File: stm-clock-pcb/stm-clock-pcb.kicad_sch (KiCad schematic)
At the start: 22 parts, among them J2 LED connector, J3 SWD, J4 USB_C_Receptacle_PowerOnly_6P, U1 STM32F103C6Tx, U2 L78L33_SOT89, Y1 16MHz

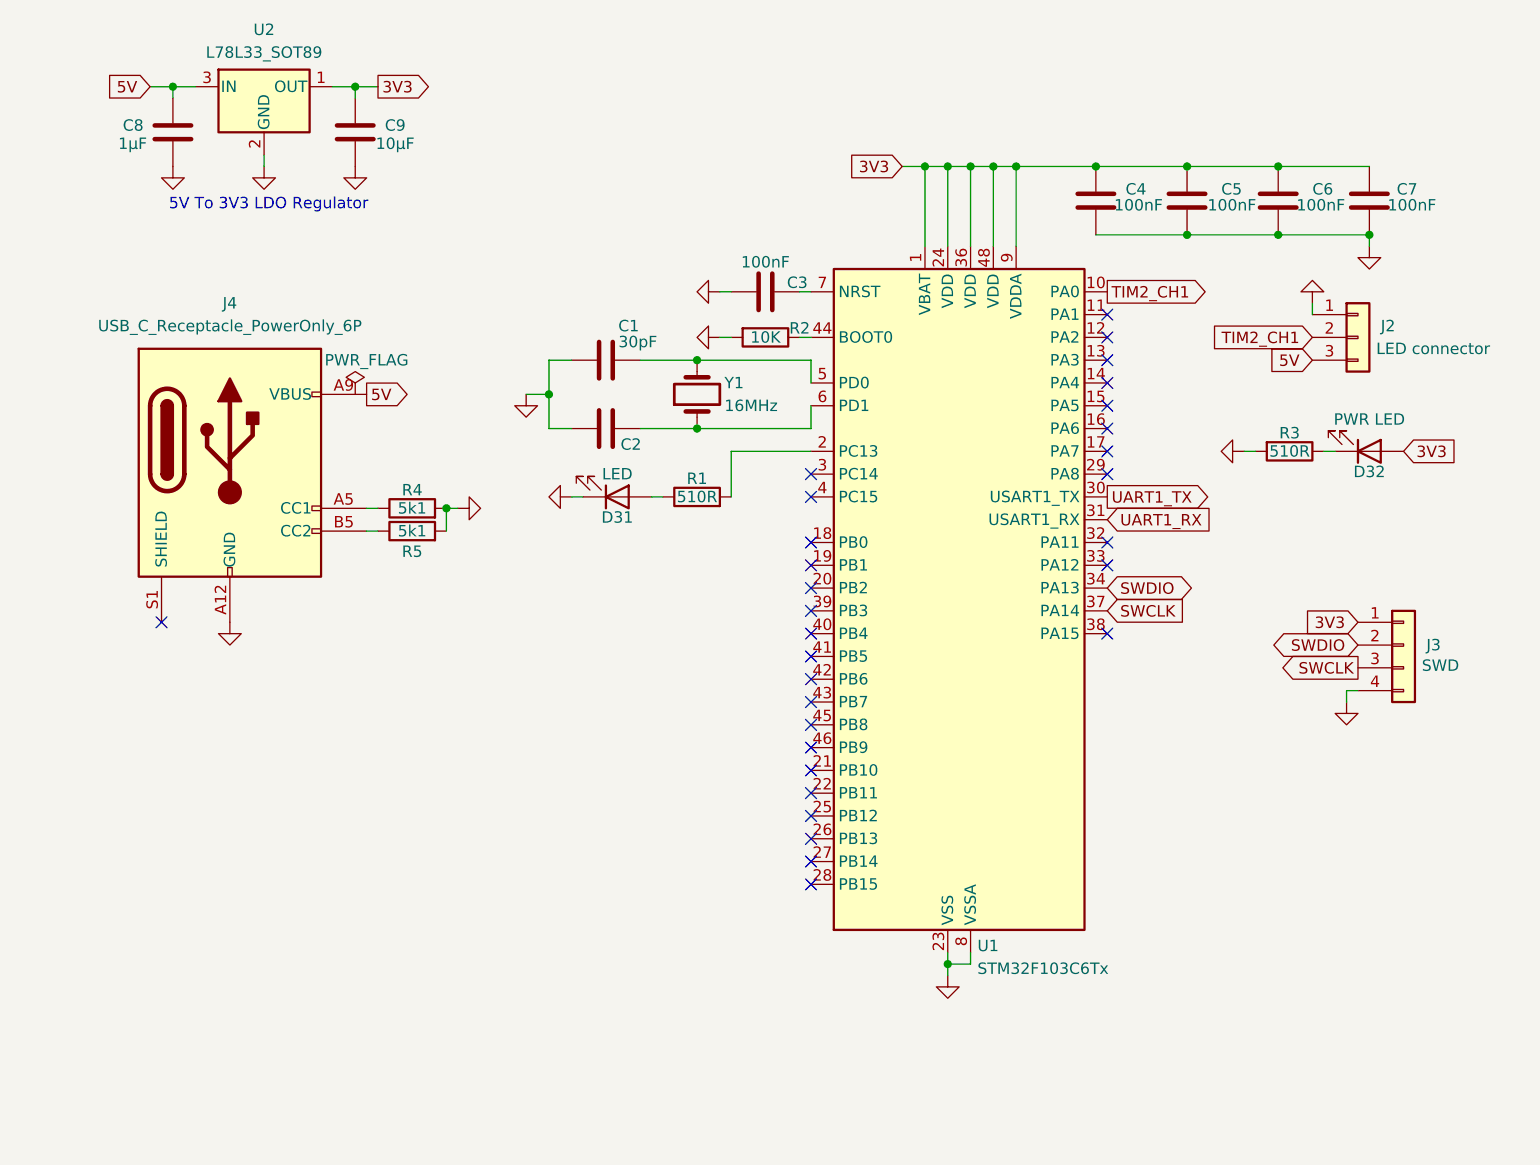
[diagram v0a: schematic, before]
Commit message: finished LED digit PCB, added gerber files, moved microcontroller kicad pcb files to different directory
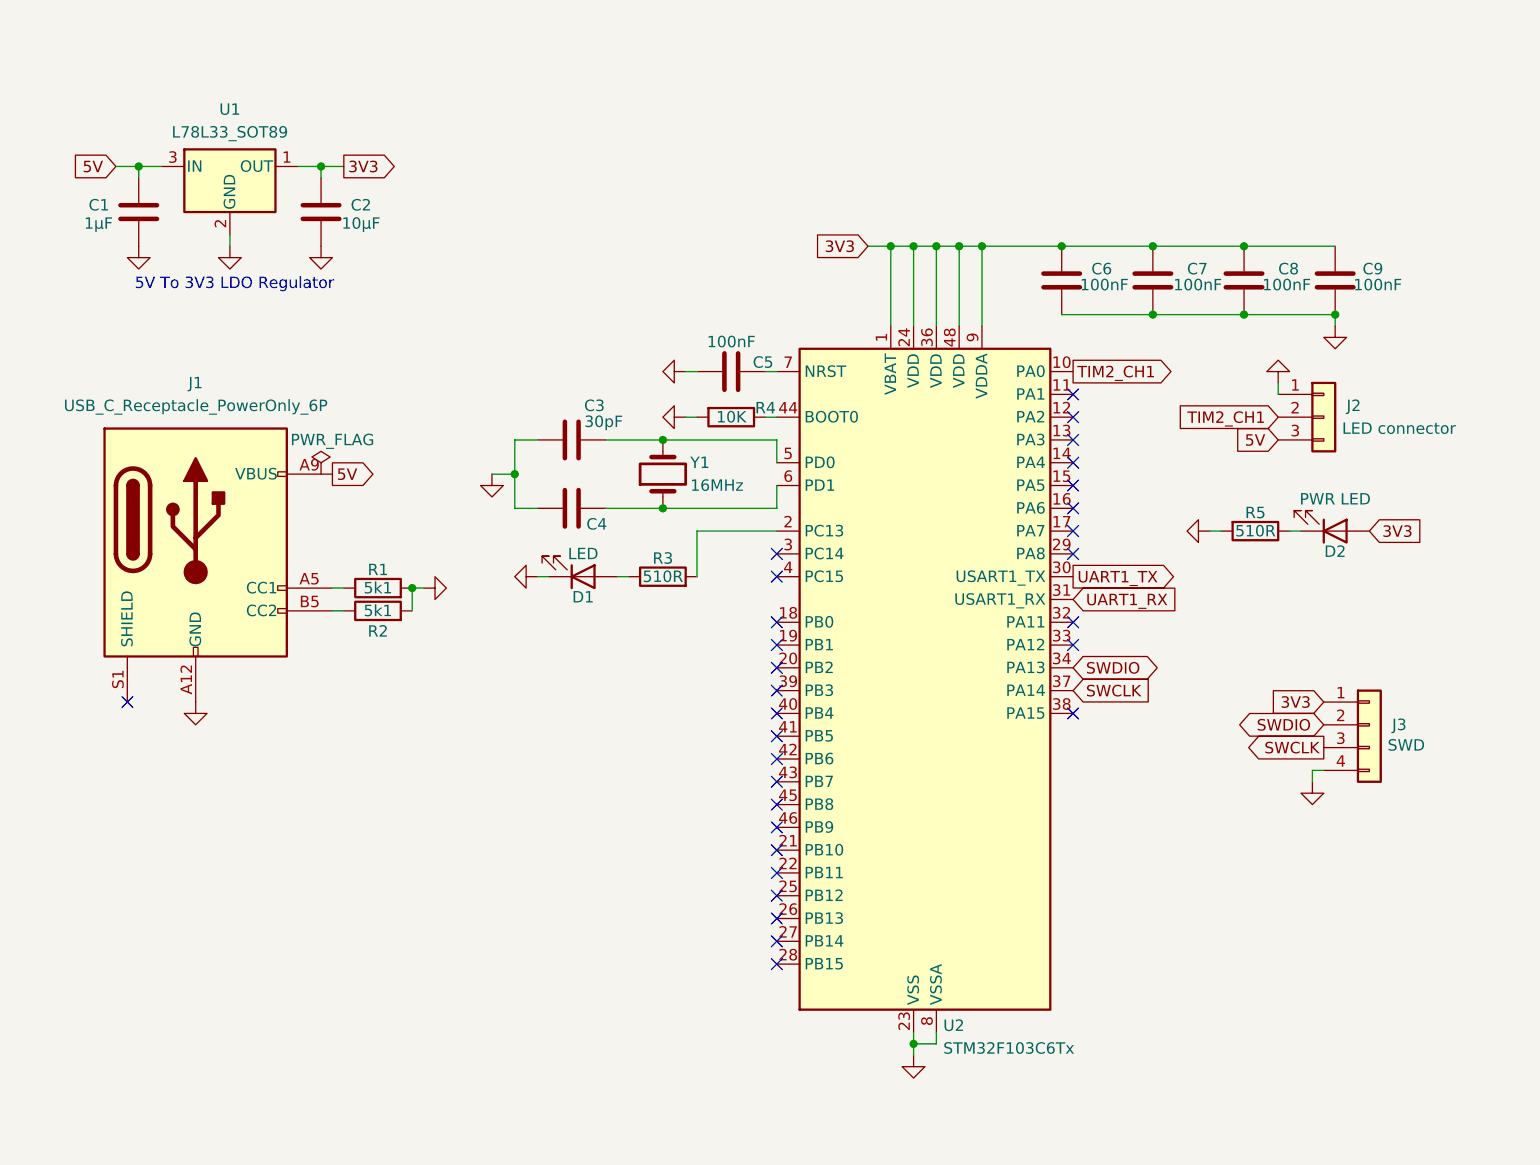
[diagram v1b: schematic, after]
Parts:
- removed D31: LED, LED_SMD:LED_0805_2012Metric, symbol Device:LED
- removed D32: PWR LED, LED_SMD:LED_0805_2012Metric, symbol Device:LED
- removed J4: USB_C_Receptacle_PowerOnly_6P, symbol Connector:USB_C_Receptacle_PowerOnly_6P
- removed U1: STM32F103C6Tx, Package_QFP:LQFP-48_7x7mm_P0.5mm, symbol MCU_ST_STM32F1:STM32F103C6Tx
- removed U2: L78L33_SOT89, Package_TO_SOT_SMD:SOT-89-3, symbol Regulator_Linear:L78L33_SOT89
- added D1: LED, LED_SMD:LED_0805_2012Metric, symbol Device:LED
- added D2: PWR LED, LED_SMD:LED_0805_2012Metric, symbol Device:LED
- added J1: USB_C_Receptacle_PowerOnly_6P, symbol Connector:USB_C_Receptacle_PowerOnly_6P
- added U1: L78L33_SOT89, Package_TO_SOT_SMD:SOT-89-3, symbol Regulator_Linear:L78L33_SOT89
- added U2: STM32F103C6Tx, Package_QFP:LQFP-48_7x7mm_P0.5mm, symbol MCU_ST_STM32F1:STM32F103C6Tx
- C1: value 30pF -> 1μF
- C2: value 30pF -> 10μF
- C3, C4: value 100nF -> 30pF; footprint Capacitor_SMD:C_0603_1608Metric -> Capacitor_SMD:C_0805_2012Metric
- C8: value 1μF -> 100nF; footprint Capacitor_SMD:C_0805_2012Metric -> Capacitor_SMD:C_0603_1608Metric
- C9: value 10μF -> 100nF; footprint Capacitor_SMD:C_0805_2012Metric -> Capacitor_SMD:C_0603_1608Metric
- R1: value 510R -> 5k1; footprint Resistor_SMD:R_0805_2012Metric -> (none)
- R2: value 10K -> 5k1; footprint Resistor_SMD:R_0805_2012Metric -> (none)
- R4: value 5k1 -> 10K; footprint (none) -> Resistor_SMD:R_0805_2012Metric
- R5: value 5k1 -> 510R; footprint (none) -> Resistor_SMD:R_0805_2012Metric
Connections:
- net 3V3: now also C2.1, C8.1, D2.2 (A), U1.1 (OUT), U2.1 (VBAT), U2.24 (VDD), U2.36 (VDD), U2.48 (VDD), U2.9 (VDDA); no longer C4.1, C5.1
- net 5V: now also C1.1, J1.A9 (VBUS), J1.B9 (VBUS), U1.3 (IN); no longer C8.1
- net GND: now also C1.2, C2.2, C4.1, C5.1, R1.2, D1.1 (K), J1.A12 (GND), J1.B12 (GND), U1.2 (GND), U2.23 (VSS), U2.35 (VSS), U2.47 (VSS), U2.8 (VSSA); no longer C1.1, C2.1, C4.2, C5.2, R3.2
- net SWCLK: now also U2.37 (PA14)
- net SWDIO: now also U2.34 (PA13)
- net TIM2_CH1: now also U2.10 (PA0)
- net UART1_RX: now also U2.31 (PA10)
- net UART1_TX: now also U2.30 (PA9)
- net at Y1.2: now also C3.2, U2.5 (PD0); no longer C1.2
- net at R3.1: now also D1.2 (A)
- net at Y1.1: now also C4.2, U2.6 (PD1); no longer C2.2
- net at R4.1: now also U2.44 (BOOT0)
- net at R5.1: now also D2.1 (K)
- net at R2.1: now also J1.B5 (CC2)
- net at R1.1: now also J1.A5 (CC1)
- new net: R3.2, U2.2 (PC13)
- new net: C5.2, U2.7 (NRST)

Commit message: added fastapi libraries & requirements list for it
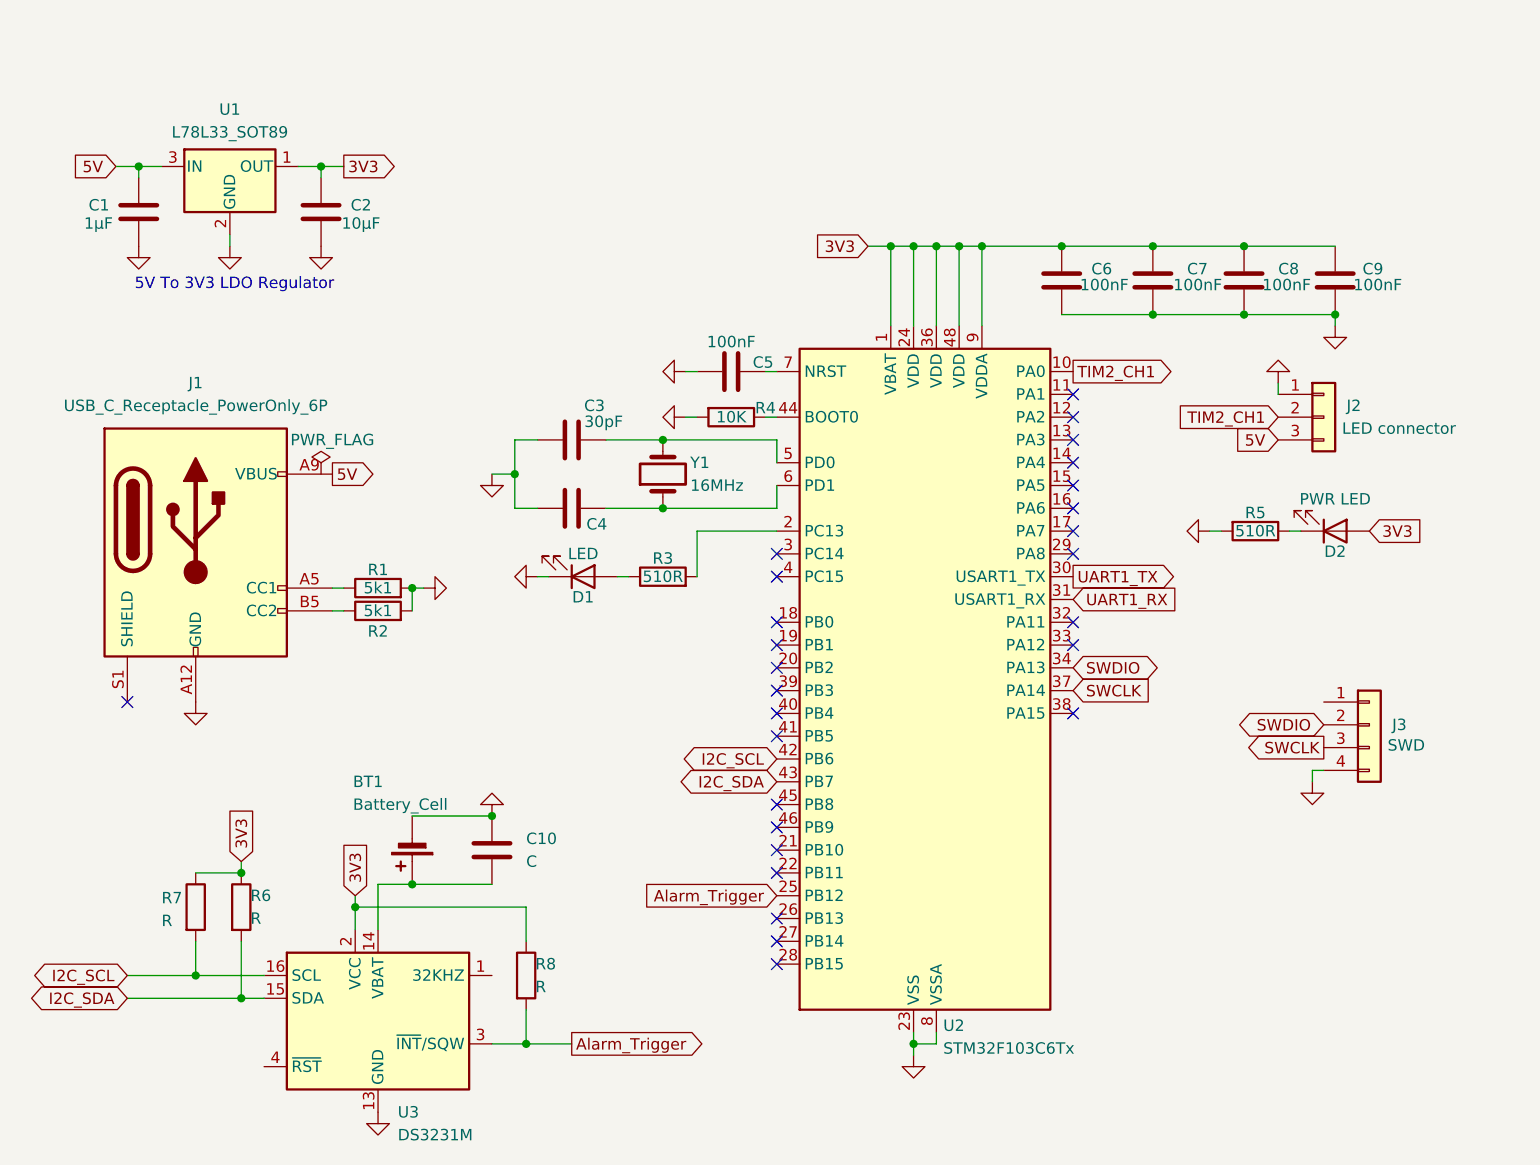
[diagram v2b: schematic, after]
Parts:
- added BT1: Battery_Cell, symbol Device:Battery_Cell
- added C10: C, symbol Device:C
- added R6, R7, R8: R, symbol Device:R
- added U3: DS3231M, Package_SO:SOIC-16W_7.5x10.3mm_P1.27mm, symbol Timer_RTC:DS3231M
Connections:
- net 3V3: now also R6.1, R7.1, R8.1, U3.2 (VCC); no longer J3.1 (Pin_1)
- net GND: now also BT1.2 (-), C10.1, U3.10 (GND), U3.11 (GND), U3.12 (GND), U3.13 (GND), U3.5 (GND), U3.6 (GND), U3.7 (GND), U3.8 (GND), U3.9 (GND)
- net Alarm_Trigger: now reaches U2.25 (PB12)
- net Alarm_Trigger: now also R8.2, U3.3 (~{INT}/SQW)
- net I2C_SCL: now reaches U2.42 (PB6)
- net I2C_SCL: now also R7.2, U3.16 (SCL)
- net I2C_SDA: now reaches U2.43 (PB7)
- net I2C_SDA: now also R6.2, U3.15 (SDA)
- new net: BT1.1 (+), C10.2, U3.14 (VBAT)
- no-connect marks 30 -> 27
